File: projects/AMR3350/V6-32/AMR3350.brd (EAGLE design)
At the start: 100 x 87 mm, 244 parts, among them IC1 LDO-TS1117CW-3V3, IC10 TMC21X0-LA, IC11 74LS32D, IC2 ATSAM4S8C, IC3 SI87XXIS, IC4 74HC125, IC5 74S08D, IC6 TMC21X0-LA, IC7 TMC21X0-LA, IC8 TMC21X0-LA, IC9 TMC21X0-LA, J1 MOLEX-105162-001, J2 MSTBV4, Q1 NX138BKS, Q2 NX138BKS, Q3 BUK9Y53-100B, Q4 BUK9Y53-100B, U1 A4403, X1 USB-B_TH, X2 12MHz, X3 KK-254-2, X4 KK-254-4, X5 KK-254-4, X6 KK-254-4, X7 KK-254-4, X8 KK-254-4, X9 KK-254-4

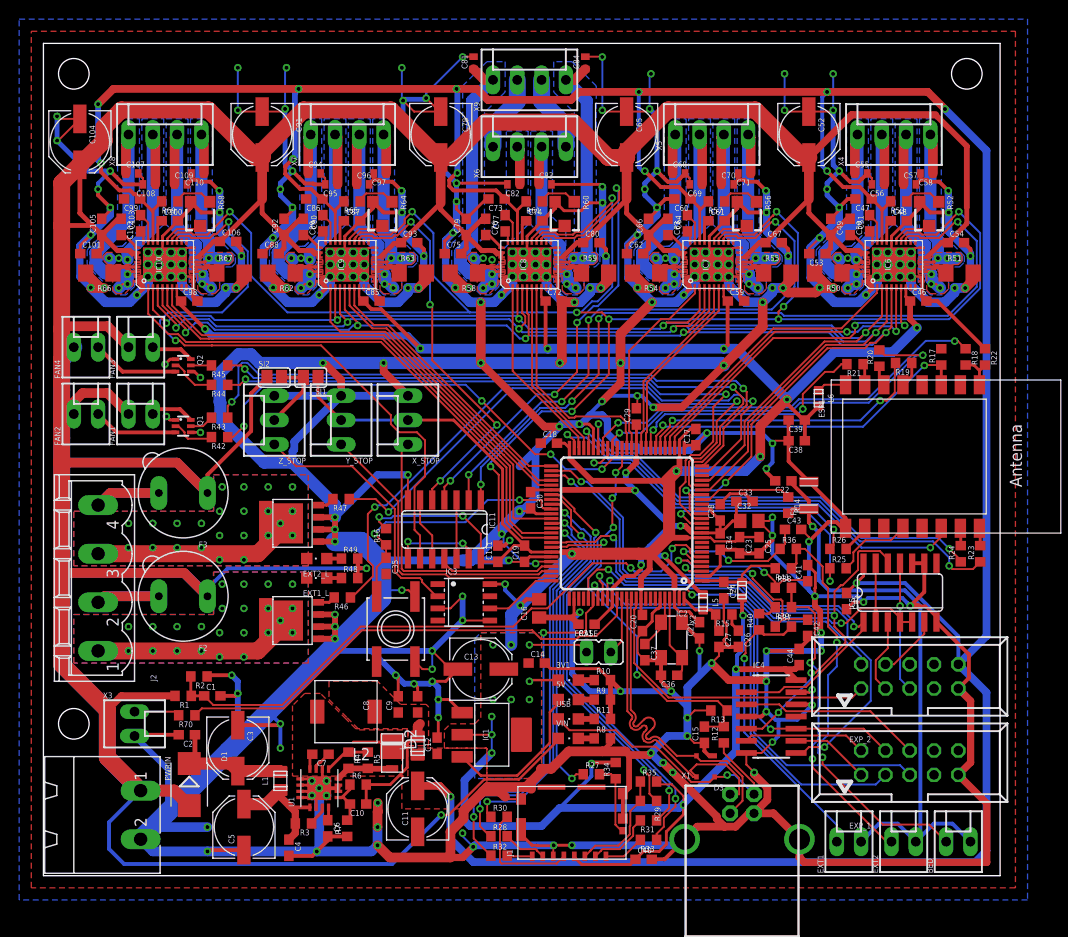
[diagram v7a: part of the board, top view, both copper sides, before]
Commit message: Properly positioned names/labels (silkscreen)
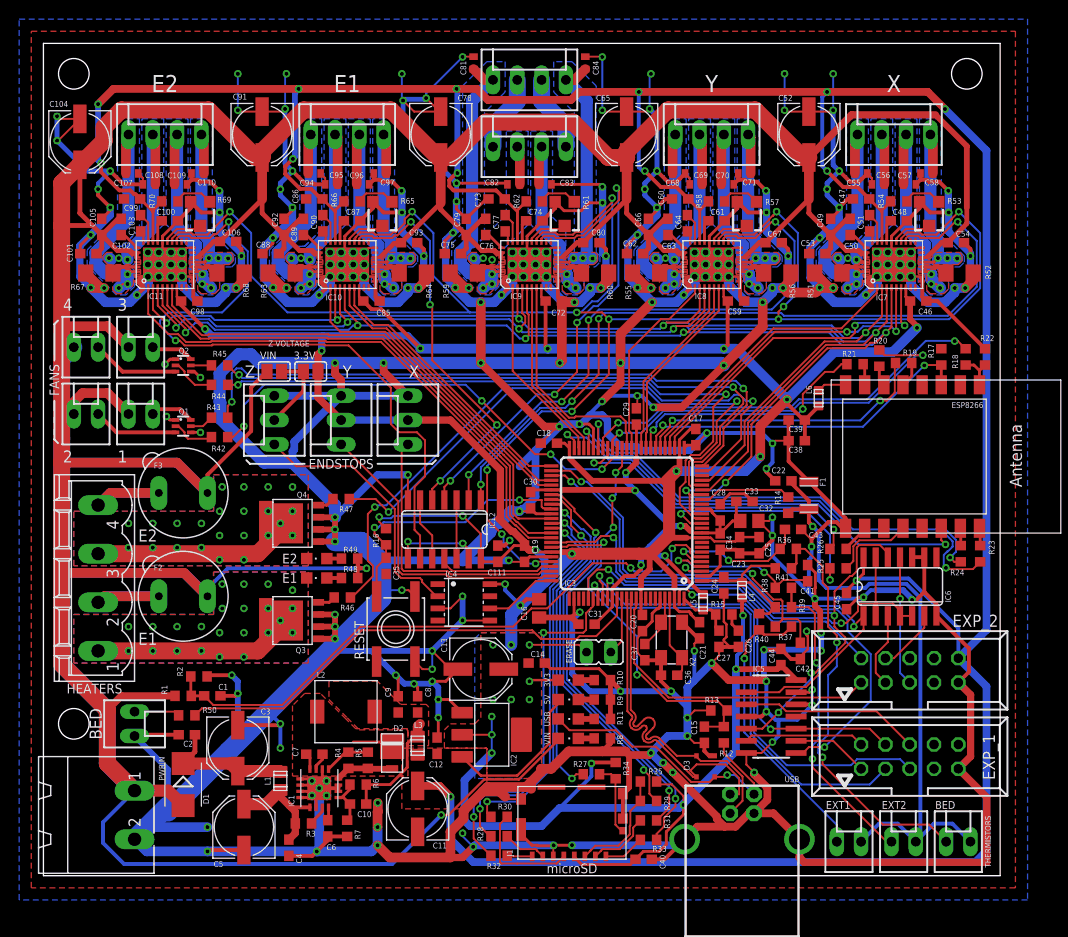
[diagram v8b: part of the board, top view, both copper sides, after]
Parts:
- removed U1: A4403, misc:QFN16-4X4
- removed X1: USB-B_TH, SmartPrj:PN61729
- added IC12: 74LS32D, 74xx-us:SO14
- added USB_L: (no value), led:CHIPLED_0805
- IC1: value LDO-TS1117CW-3V3 -> A4403; device we-power:SOT223 -> misc:QFN16-4X4
- IC11: value 74LS32D -> TMC21X0-LA; device 74xx-us:SO14 -> SilentStepStick-TMC2130_v11:QFN36-PAD
- IC2: value ATSAM4S8C -> LDO-TS1117CW-3V3; device misc:LQFP100 -> we-power:SOT223
- IC3: value SI87XXIS -> ATSAM4S8C; device misc:SOIC08-FAIRCHILD -> misc:LQFP100
- IC4: value 74HC125 -> SI87XXIS; device misc:SO14 -> misc:SOIC08-FAIRCHILD
- IC5: value 74S08D -> 74HC125; device 74xx-us:SO14 -> misc:SO14
- IC6: value TMC21X0-LA -> 74S08D; device SilentStepStick-TMC2130_v11:QFN36-PAD -> 74xx-us:SO14
- R50: value 0R11 -> 180R; device resistor:R1206 -> resistor:R0603
- R52, R56, R60, R64, R68: value 20K -> 0R11; device resistor:RTRIM3103 -> resistor:R1206
- R53, R57, R61, R65, R69: device resistor:R0603 -> resistor:RTRIM3103
- R54, R58, R62, R66: value 0R11 -> 20K; device resistor:R1206 -> resistor:R0603
- R70: value 180R -> 20K
- USB: value (none) -> USB-B_TH; device led:CHIPLED_0805 -> SmartPrj:PN61729
- moved R50 81.4 mm to (15.0, 16.8)
- moved R70 53.8 mm to (13.2, 70.5)
- moved IC11 40.2 mm to (12.7, 63.9), turned to 90 degrees
- moved X9 38.5 mm to (12.7, 77.5)
- moved IC4 34.3 mm to (43.9, 28.6)
- moved IC6 33.7 mm to (89.5, 30.2), turned to 0 degrees
- moved R54 27.5 mm to (89.4, 70.5)
- moved R58 27.5 mm to (70.4, 70.5)
- moved R66 27.5 mm to (32.3, 70.5)
- moved R62 27.5 mm to (51.3, 70.5)
- moved IC2 26.2 mm to (46.9, 14.7), turned to 0 degrees
- moved USB 22.1 mm to (73.0, 3.81), turned to 0 degrees
- moved X7 19.9 mm to (50.8, 83.2)
- moved IC7 19.1 mm to (88.9, 63.9)
- moved IC10 19.1 mm to (31.8, 63.9)
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- renumbered 3V1 to 3V3, ESP1 to ESP8266
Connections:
- net ESP_URDX renamed ESP_RXD
- net ESP_UTDX renamed ESP_TXD
- net N$1 renamed E1_FUSED
- net N$2 renamed E2_FUSED
- net N$55 renamed IDEK
- removed net N$3: X6.1, X9.2
- removed net N$4: X6.4, X9.3
- removed net N$5: IC11.10, IC11.6
- removed net N$7: IC11.12, IC11.3
- removed net N$8: IC11.13, IC11.8
- new net AMID_Z: X6.1, X7.2
- new net BMID_Z: X6.4, X7.3
- new net SG_TST_E1Z: IC12.10, IC12.6
- new net SG_TST_XY: IC12.12, IC12.3
- new net SG_TST_ZE: IC12.13, IC12.8
- net +12V: now also IC11.16, IC11.30, IC11.31; no longer IC6.16, IC6.30, IC6.31
- net +3V3: now also IC11.8, IC12.14, IC2.2, IC2.4, IC3.10, IC3.27, IC3.50, IC3.69, IC3.91, IC3.98, IC4.8, IC5.14; no longer IC1.2, IC1.4, IC11.14, IC2.10, IC2.27, IC2.50, IC2.69, IC2.91, IC2.98, IC3.8, IC4.14, IC6.8
- net +5V: now also IC11.26, IC2.3, IC6.14, R54.2, R58.2, R62.2, R66.2, R70.2; no longer IC1.3, IC5.14, IC6.26, R53.2, R57.2, R61.2, R65.2, R69.2
- net 5V_E1: now also IC10.25; no longer IC9.25
- net 5V_E2: now also IC11.25; no longer IC10.25
- net 5V_X: now also IC7.25; no longer IC6.25
- net 5V_Y: now also IC8.25; no longer IC7.25
- net 5V_Z: now also IC9.25; no longer IC8.25
- net A1_E1: now also IC10.34, X8.1; no longer IC9.34, X7.1
- net A1_E2: now also IC11.34, X9.1; no longer IC10.34, X8.1
- net A1_X: now also IC7.34; no longer IC6.34
- net A1_Y: now also IC8.34; no longer IC7.34
- net A1_Z: now also IC9.34, X7.1; no longer IC8.34, X9.1
- net A2_E1: now also IC10.32, X8.2; no longer IC9.32, X7.2
- net A2_E2: now also IC11.32, X9.2; no longer IC10.32, X8.2
- net A2_X: now also IC7.32; no longer IC6.32
- net A2_Y: now also IC8.32; no longer IC7.32
- net A2_Z: now also IC9.32; no longer IC8.32
- net ADVREF: now also IC3.1; no longer IC2.1
- net B1_E1: now also IC10.13, X8.3; no longer IC9.13, X7.3
- net B1_E2: now also IC11.13, X9.3; no longer IC10.13, X8.3
- net B1_X: now also IC7.13; no longer IC6.13
- net B1_Y: now also IC8.13; no longer IC7.13
- net B1_Z: now also IC9.13; no longer IC8.13
- net B2_E1: now also IC10.15, X8.4; no longer IC9.15, X7.4
- net B2_E2: now also IC11.15, X9.4; no longer IC10.15, X8.4
- net B2_X: now also IC7.15; no longer IC6.15
- net B2_Y: now also IC8.15; no longer IC7.15
- net B2_Z: now also IC9.15, X7.4; no longer IC8.15, X9.4
- net BED: now also IC3.86, R50.1; no longer IC2.86, R70.1
- net BED_OUT: now also R50.2; no longer R70.2
- net BOOT: now also IC1.11; no longer U1.11
- net BRA_E1: now also IC10.33, R63.1; no longer IC9.33, R62.1
- net BRA_E2: now also IC11.33, R67.1; no longer IC10.33, R66.1
- net BRA_X: now also IC7.33, R51.1; no longer IC6.33, R50.1
- net BRA_Y: now also IC8.33, R55.1; no longer IC7.33, R54.1
- net BRA_Z: now also IC9.33, R59.1; no longer IC8.33, R58.1
- net BRB_E1: now also IC10.14, R64.1; no longer IC9.14, R63.1
- net BRB_E2: now also IC11.14, R68.1; no longer IC10.14, R67.1
- net BRB_X: now also IC7.14, R52.1; no longer IC6.14, R51.1
- net BRB_Y: now also IC8.14, R56.1; no longer IC7.14, R55.1
- net BRB_Z: now also IC9.14, R60.1; no longer IC8.14, R59.1
- net CPI_E1: now also IC10.28; no longer IC9.28
- net CPI_E2: now also IC11.28; no longer IC10.28
- net CPI_X: now also IC7.28; no longer IC6.28
- net CPI_Y: now also IC8.28; no longer IC7.28
- net CPI_Z: now also IC9.28; no longer IC8.28
- net CPO_E1: now also IC10.27; no longer IC9.27
- net CPO_E2: now also IC11.27; no longer IC10.27
- net CPO_X: now also IC7.27; no longer IC6.27
- net CPO_Y: now also IC8.27; no longer IC7.27
- net CPO_Z: now also IC9.27; no longer IC8.27
- net E1_DIR: now also IC10.7, IC3.51; no longer IC2.51, IC9.7
- net E1_EN: now also IC10.2, IC3.55; no longer IC2.55, IC9.2
- net E1_STEP: now also IC10.6, IC3.54; no longer IC2.54, IC9.6
- net E2_DIR: now also IC11.7, IC3.62; no longer IC10.7, IC2.62
- net E2_EN: now also IC11.2, IC3.66; no longer IC10.2, IC2.66
- net E2_STEP: now also IC11.6, IC3.65; no longer IC10.6, IC2.65
- net ENN: now also IC11.22, IC3.71; no longer IC2.71, IC6.22
- net ERASE: now also IC3.87; no longer IC2.87
- net ESP_DATA_RDY: now also IC3.13; no longer IC2.13
- net ESP_EN: now also IC3.32; no longer IC2.32
- net ESP_MISO: now also IC3.41; no longer IC2.41
- net ESP_MOSI: now also IC3.33; no longer IC2.33
- net ESP_NPCS0: now also IC3.42; no longer IC2.42
- net ESP_RESET: now also IC3.43; no longer IC2.43
- net ESP_SCK: now also IC3.31; no longer IC2.31
- net ESP_URXD: now also IC3.46; no longer IC2.46
- net ESP_UTXD: now also IC3.44; no longer IC2.44
- net EXT1: now also IC3.24; no longer IC2.24
- net EXT2: now also IC3.19; no longer IC2.19
- net FAN_E1: now also IC3.40; no longer IC2.40
- net FAN_E2: now also IC3.25; no longer IC2.25
- net FAN_MOBO: now also IC3.14; no longer IC2.14
- net FAN_PART: now also IC3.21; no longer IC2.21
- net FB: now also IC1.5; no longer U1.5
- net GND: now also IC1.10, IC1.13, IC1.14, IC1.15, IC1.16, IC1.2, IC1.6, IC1.7, IC1.EXP, IC11.1, IC11.11, IC11.12, IC11.18, IC11.24, IC11.35, IC11.36, IC11.TP, IC12.7, IC2.1, IC3.2, IC3.26, IC3.45, IC3.61, IC3.70, IC3.77, IC3.95, IC4.3, IC4.5, IC5.1, IC5.12, IC5.13, IC5.4, IC6.10, IC6.7, IC6.9, R52.2, R53.3, R56.2, R57.3, R60.2, R61.3, R64.2, R65.3, R68.2, R69.3, USB.4, USB.P$1, USB.P$2; no longer IC1.1, IC11.7, IC2.2, IC2.26, IC2.45, IC2.61, IC2.70, IC2.77, IC2.95, IC3.3, IC3.5, IC4.1, IC4.12, IC4.13, IC4.4, IC4.7, IC5.10, IC5.9, IC6.1, IC6.11, IC6.12, IC6.18, IC6.24, IC6.35, IC6.36, IC6.TP, R50.2, R52.3, R54.2, R56.3, R58.2, R60.3, R62.2, R64.3, R66.2, R68.3, U1.10, U1.13, U1.14, U1.15, U1.16, U1.2, U1.6, U1.7, U1.EXP, X1.4, X1.P$1, X1.P$2
- net IREF_E1: now also IC10.23, R65.2; no longer IC9.23, R64.2
- net IREF_E2: now also IC11.23, R69.2; no longer IC10.23, R68.2
- net IREF_X: now also IC7.23, R53.2; no longer IC6.23, R52.2
- net IREF_Y: now also IC8.23, R57.2; no longer IC7.23, R56.2
- net IREF_Z: now also IC9.23, R61.2; no longer IC8.23, R60.2
- net ISEN: now also IC1.8; no longer U1.8
- net LCD_BEEP: now also IC3.90; no longer IC2.90
- net LCD_CS: now also IC3.80, IC6.13, IC6.2, IC6.4, IC6.5; no longer IC2.80, IC5.13, IC5.2, IC5.4, IC5.5
- net LCD_CS_BUF: now also IC6.6; no longer IC5.6
- net LCD_ENC_A: now also IC3.83; no longer IC2.83
- net LCD_ENC_B: now also IC3.82; no longer IC2.82
- net LCD_ENC_SW: now also IC3.84; no longer IC2.84
- net LCD_MISO: now also IC3.53, IC5.8; no longer IC2.53, IC4.8
- net LCD_MISO_BUF: now also IC5.9; no longer IC4.9
- net LCD_MOSI: now also IC3.52, IC5.2, IC6.1; no longer IC2.52, IC4.2, IC5.1
- net LCD_MOSI_BUF: now also IC6.3; no longer IC5.3
- net LCD_SCK: now also IC3.67, IC5.5, IC6.12; no longer IC2.67, IC4.5, IC5.12
- net LCD_SCK_BUF: now also IC6.11; no longer IC5.11
- net LCD_SD_CS: now also IC3.99, IC5.10; no longer IC2.99, IC4.10
- net LX: now also IC1.12; no longer U1.12
- net MCCDA: now also IC3.59; no longer IC2.59
- net MCCK: now also IC3.63; no longer IC2.63
- net MCDA0: now also IC3.64; no longer IC2.64
- net MCDA1: now also IC3.81; no longer IC2.81
- net MCDA2: now also IC3.39; no longer IC2.39
- net MCDA3: now also IC3.57; no longer IC2.57
- net MOT_MISO: now also IC11.5, IC3.15; no longer IC2.15, IC6.5
- net MOT_MOSI: now also IC11.4, IC3.20; no longer IC2.20, IC6.4
- net MOT_SCK: now also IC11.3, IC3.22; no longer IC2.22, IC6.3
- net PWR_FAIL_DET2: now also IC3.6; no longer IC2.6
- net REFIN_E1: now also R66.1; no longer R64.1
- net REFIN_E2: now also R70.1; no longer R68.1
- net REFIN_X: now also R54.1; no longer R52.1
- net REFIN_Y: now also R58.1; no longer R56.1
- net REFIN_Z: now also R62.1; no longer R60.1
- net RESET: now also IC3.60; no longer IC2.60
- net SAM_TFR_RDY: now also IC3.49; no longer IC2.49
- net SD_CD: now also IC3.58; no longer IC2.58
- net SD_MOSI_BUF: now also IC5.3; no longer IC4.3
- net SD_SCK_BUF: now also IC5.6; no longer IC4.6
- net SGND: now also IC1.9; no longer U1.9
- net SG_TST: now also IC12.11, IC3.72; no longer IC11.11, IC2.72
- net SG_TST_E1: now also IC10.21, IC12.5; no longer IC11.5, IC9.21
- net SG_TST_E2: now also IC11.21, IC12.9; no longer IC10.21, IC11.9
- net SG_TST_X: now also IC12.1, IC7.21; no longer IC11.1, IC6.21
- net SG_TST_Y: now also IC12.2, IC8.21; no longer IC11.2, IC7.21
- net SG_TST_Z: now also IC12.4, IC9.21; no longer IC11.4, IC8.21
- net SS: now also IC1.4; no longer U1.4
- net TON: now also IC1.3; no longer U1.3
- net T_BED: now also IC3.5; no longer IC2.5
- net T_EXT1: now also IC3.3; no longer IC2.3
- net T_EXT2: now also IC3.4; no longer IC2.4
- net USB_LED: now also USB_L.C; no longer USB.C
- net USB_N: now also IC3.88, USB.2; no longer IC2.88, X1.2
- net USB_P: now also IC3.89, USB.3; no longer IC2.89, X1.3
- net USB_PWR_MON: now also IC3.68; no longer IC2.68
- net VBUS: now also USB.1, USB_L.A; no longer USB.A, X1.1
- net VCP_E1: now also IC10.29; no longer IC9.29
- net VCP_E2: now also IC11.29; no longer IC10.29
- net VCP_X: now also IC7.29; no longer IC6.29
- net VCP_Y: now also IC8.29; no longer IC7.29
- net VCP_Z: now also IC9.29; no longer IC8.29
- net VDDOUT: now also IC3.11, IC3.16, IC3.36, IC3.56, IC3.85; no longer IC2.11, IC2.16, IC2.36, IC2.56, IC2.85
- net VDDPLL: now also IC3.100; no longer IC2.100
- net VIN_F: now also IC1.1; no longer U1.1
- net VREF_MON: now also IC3.12; no longer IC2.12
- net VSSA_MON: now also IC3.18; no longer IC2.18
- net XIN: now also IC3.97; no longer IC2.97
- net XOUT: now also IC3.96; no longer IC2.96
- net X_DIR: now also IC3.28, IC7.7; no longer IC2.28, IC6.7
- net X_EN: now also IC3.30, IC7.2; no longer IC2.30, IC6.2
- net X_STEP: now also IC3.29, IC7.6; no longer IC2.29, IC6.6
- net X_STOP: now also IC3.73; no longer IC2.73
- net Y_DIR: now also IC3.34, IC8.7; no longer IC2.34, IC7.7
- net Y_EN: now also IC3.37, IC8.2; no longer IC2.37, IC7.2
- net Y_STEP: now also IC3.35, IC8.6; no longer IC2.35, IC7.6
- net Y_STOP: now also IC3.74; no longer IC2.74
- net Z_DIR: now also IC3.38, IC9.7; no longer IC2.38, IC8.7
- net Z_EN: now also IC3.48, IC9.2; no longer IC2.48, IC8.2
- net Z_STEP: now also IC3.47, IC9.6; no longer IC2.47, IC8.6
- net Z_STOP: now also IC3.75, IC4.6; no longer IC2.75, IC3.6
- net Z_STOP_IN: now also IC4.2; no longer IC3.2
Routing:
- net SG_TST_ZE: track 0.00 -> 9.49 mm, vias 0 -> 2
- net N$8: track 9.49 -> 0.00 mm, vias 2 -> 0
- net N$4: track 8.04 -> 0.00 mm
- net BMID_Z: track 0.00 -> 8.04 mm
- net N$3: track 8.04 -> 0.00 mm
- net AMID_Z: track 0.00 -> 8.04 mm
- net +3V3: track 394.3 -> 402.0 mm, vias 27 -> 29
- net SG_TST_E1Z: track 0.00 -> 6.67 mm
- net N$5: track 6.67 -> 0.00 mm
- net SG_TST_XY: track 0.00 -> 6.15 mm
- net N$7: track 6.15 -> 0.00 mm
- net GND: track 1443.2 -> 1447.8 mm, vias 223 -> 224
- net ESP_URXD: track 49.8 -> 52.1 mm
- net ESP_UTXD: track 47.3 -> 49.2 mm
- net SG_TST_E2: track 71.7 -> 73.5 mm
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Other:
- board text added: "1"
- board text added: "2"
- board text added: "3"
- board text added: "3.3V"
- board text added: "4"
- board text added: "BED"
- board text added: "E1"
- board text added: "E2"
- board text added: "ENDSTOPS"
- board text added: "FANS"
- board text added: "HEATERS"
- board text added: "RESET"
- board text added: "THERMISTORS"
- board text added: "USB"
- board text added: "VIN"
- board text added: "X"
- board text added: "Y"
- board text added: "Z"
- board text added: "Z VOLTAGE"
- board text added: "microSD"
